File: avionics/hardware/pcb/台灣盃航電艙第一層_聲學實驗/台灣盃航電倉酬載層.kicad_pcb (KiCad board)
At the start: 4 copper layers, 80.1 x 79.9 mm, 48 parts, among them U1 MPXV2202DPT1, U10 INA333xxDGK, U2 LM2733YMF, U3 Connector, U4 INA333xxDGK, U5 MPXV2202DPT1, U6 INA333xxDGK, U7 MPXV2202DPT1, U8 INA333xxDGK, U9 MPXV2202DPT1

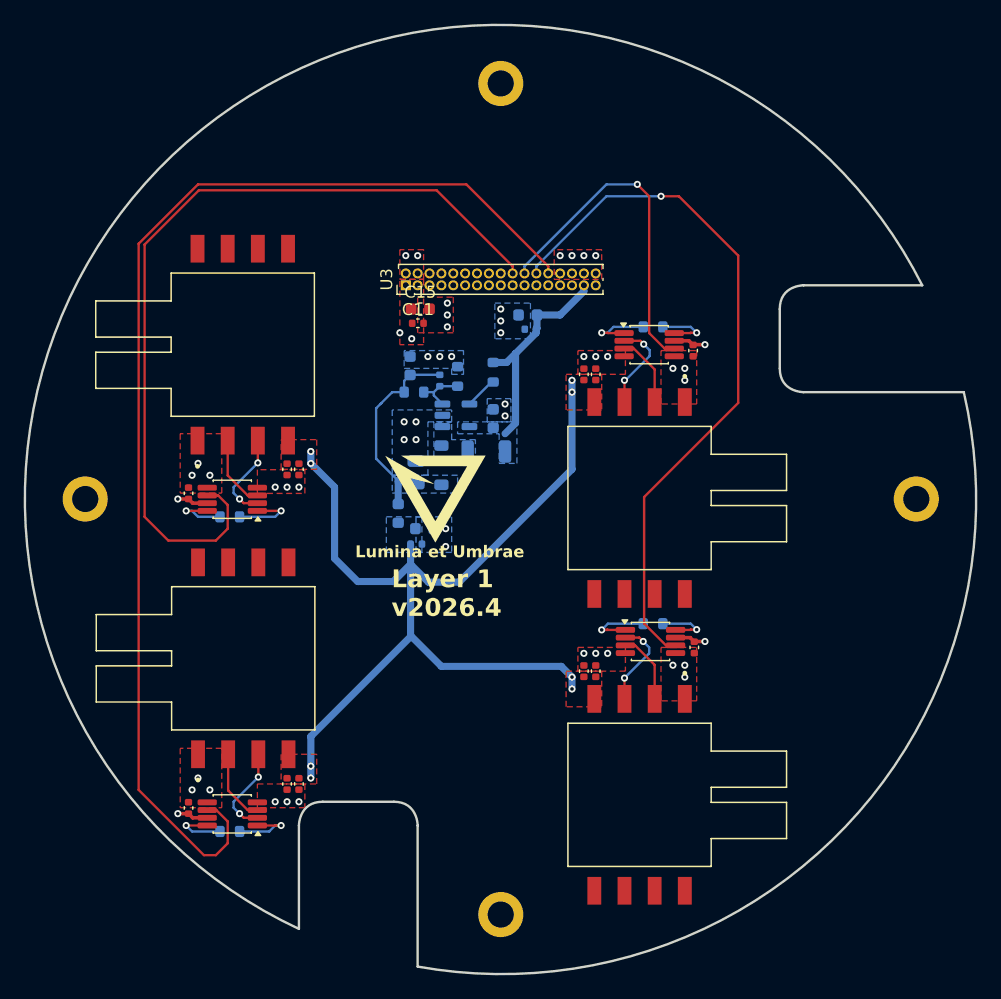
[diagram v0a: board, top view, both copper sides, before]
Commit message: 上傳新的連接器
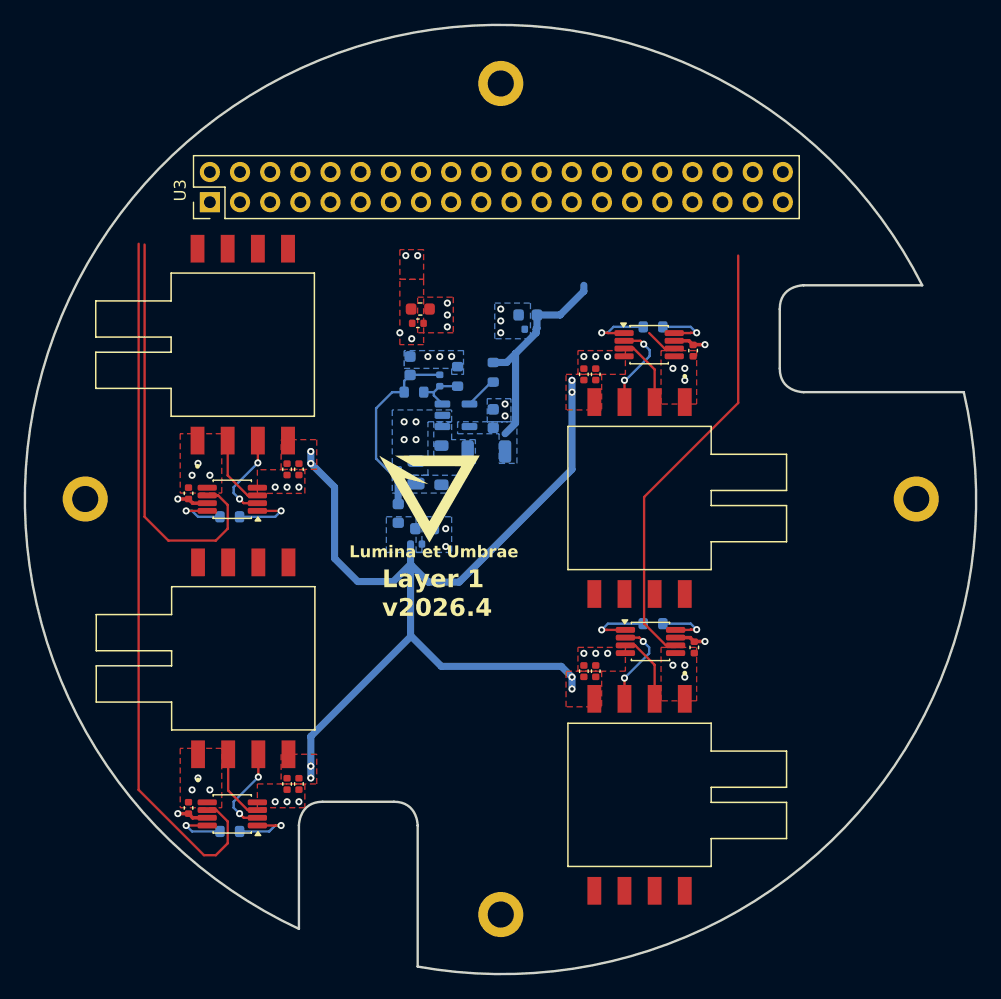
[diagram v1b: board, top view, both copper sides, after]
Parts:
- U3: footprint Connector_PinHeader_1.00mm:PinHeader_2x17_P1.00mm_Vertical -> Connector_PinHeader_2.54mm:PinHeader_2x20_P2.54mm_Vertical
- moved U3 17.9 mm to (122.5, 71.0)
- moved G*** 0.50 mm to (141.0, 94.8)
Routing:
- net PAYLOAD_4: track 100.2 -> 60.2 mm
- net PAYLOAD_1: track 71.4 -> 35.2 mm
- net PAYLOAD_2: track 28.5 -> 2.65 mm, vias 1 -> 0
- net PAYLOAD_3: track 59.8 -> 37.7 mm, vias 1 -> 0
- net GND: vias 47 -> 43

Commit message: 將第一至三層連接器修改成PC104規格，第四層還未進行
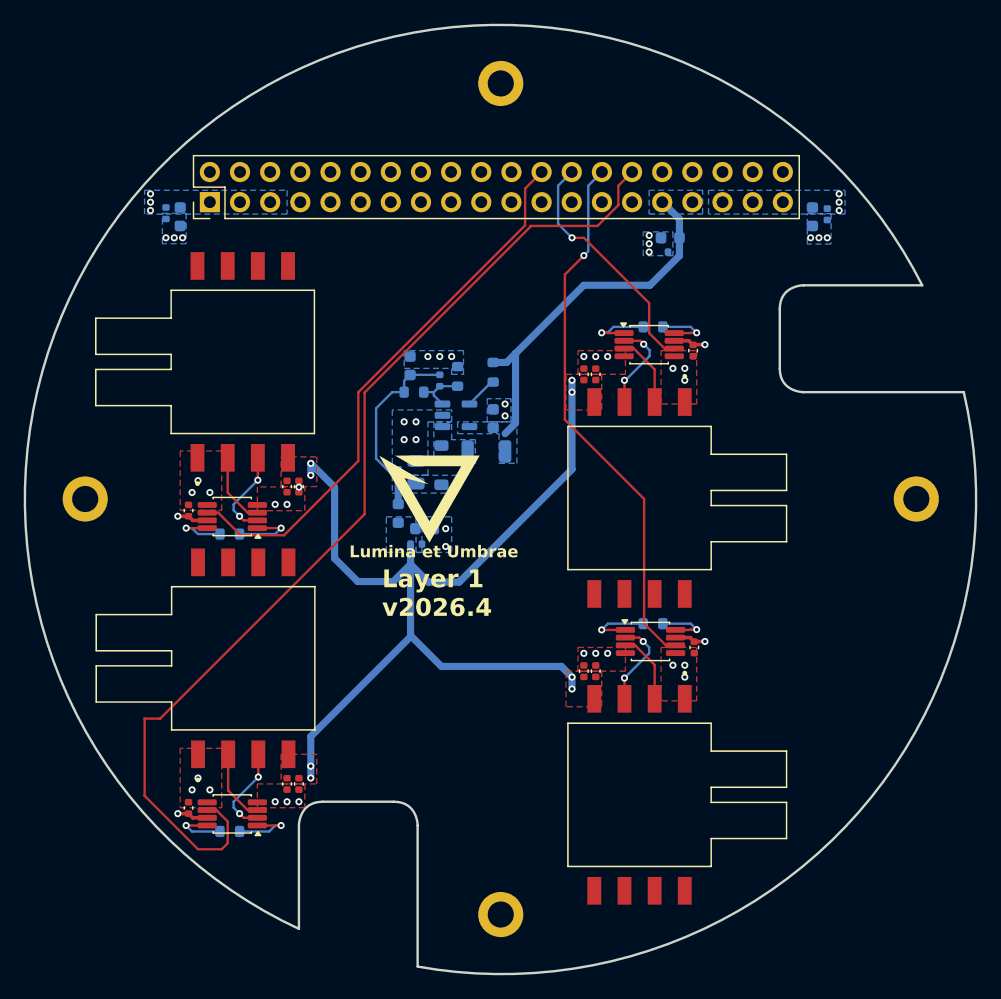
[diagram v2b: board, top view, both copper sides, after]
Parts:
- removed the C11 at (140.0, 81.2)
- removed the C15 at (140.2, 80.0)
- removed the C24 at (149.5, 81.7)
- removed the C25 at (149.3, 80.5)
- removed the U3 at (122.5, 71.0)
- added C3: 100n, Capacitor_SMD:C_0402_1005Metric, B.Cu at (118.8, 71.9)
- added C4: 100n, Capacitor_SMD:C_0402_1005Metric, B.Cu at (161.6, 75.2)
- added C5: 100n, Capacitor_SMD:C_0402_1005Metric, B.Cu at (174.5, 72.0)
- added C7: 10u, Capacitor_SMD:C_0603_1608Metric, B.Cu at (120.0, 72.2)
- added C8: 10u, Capacitor_SMD:C_0603_1608Metric, B.Cu at (161.3, 74.0)
- added C9: 10u, Capacitor_SMD:C_0603_1608Metric, B.Cu at (173.2, 72.2)
- added U5: Connector, Connector_PinHeader_2.54mm:PinHeader_2x20_P2.54mm_Vertical, F.Cu at (122.5, 71.0)
- moved C12 1.45 mm to (129.0, 95.0)
- moved C20 1.45 mm to (120.7, 97.0)
- moved C6 1.45 mm to (130.0, 95.0)
- moved R1 1.45 mm to (124.2, 99.0)
- moved U1 1.45 mm to (125.3, 84.5)
- moved U2 1.45 mm to (124.4, 97.5)
- renumbered C9 to C1, C1 to C10, C2 to C11, C8 to C12, C3 to C13, C4 to C14, C5 to C15, C12 to C16, C6 to C17, C13 to C18, C14 to C19, C16 to C2, C10 to C20, C17 to C21, C18 to C22, C20 to C23, C21 to C24, C22 to C25, C7 to C6, D2 to D1, H3 to H2, H2 to H3, L2 to L1, R3 to R1, R7 to R2, R2 to R3, R1 to R4, R4 to R5, R5 to R6, R6 to R7, U4 to U2, U2 to U3, U5 to U4
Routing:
- net PAYLOAD_4: track 60.2 -> 86.7 mm
- net PAYLOAD_2: track 2.65 -> 20.5 mm, vias 0 -> 1
- net +5V: track 18.6 -> 31.6 mm
- net PAYLOAD_1: track 35.2 -> 46.8 mm
- net PAYLOAD_3: track 37.7 -> 45.5 mm, vias 0 -> 1
- net GND: vias 43 -> 44
- net +3V3: vias 6 -> 10
- added copper zone on B.Cu, net +3V3
- removed copper zone on F.Cu, net +3V3
